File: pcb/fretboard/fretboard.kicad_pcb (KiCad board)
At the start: 2 copper layers, 46 x 186 mm, 101 parts, among them J1 Conn_01x05_Pin, J10 Conn_01x01_Pin, J11 Conn_01x01_Pin, J12 Conn_01x01_Pin, J13 Conn_01x01_Pin, J14 Conn_01x01_Pin, J15 Conn_01x01_Pin, J16 Conn_01x01_Pin, J17 Conn_01x01_Pin, J18 Conn_01x01_Pin, J19 Conn_01x01_Pin, J2 Conn_01x01_Pin, J20 Conn_01x01_Pin, J21 Conn_01x01_Pin, J22 Conn_01x01_Pin, J23 Conn_01x01_Pin, J24 Conn_01x01_Pin, J25 Conn_01x01_Pin, J26 Conn_01x01_Pin, J27 Conn_01x01_Pin, J28 Conn_01x01_Pin, J29 Conn_01x01_Pin, J3 Conn_01x01_Pin, J30 Conn_01x01_Pin, J31 Conn_01x01_Pin, J32 Conn_01x01_Pin, J33 Conn_01x01_Pin, J34 Conn_01x01_Pin, J35 Conn_01x01_Pin, J36 Conn_01x01_Pin, J37 Conn_01x01_Pin, J38 Conn_01x01_Pin, J39 Conn_01x01_Pin, J4 Conn_01x01_Pin, J40 Conn_01x01_Pin, J41 Conn_01x01_Pin, J42 Conn_01x01_Pin, J43 Conn_01x01_Pin, J44 Conn_01x01_Pin, J45 Conn_01x01_Pin, J46 Conn_01x01_Pin, J47 Conn_01x01_Pin, J48 Conn_01x01_Pin, J49 Conn_01x01_Pin, J5 Conn_01x01_Pin, J50 Conn_01x01_Pin, J51 Conn_01x01_Pin, J52 Conn_01x01_Pin, J53 Conn_01x01_Pin, J54 Conn_01x01_Pin, J55 Conn_01x01_Pin, J56 Conn_01x01_Pin, J57 Conn_01x01_Pin, J58 Conn_01x01_Pin, J59 Conn_01x01_Pin, J6 Conn_01x01_Pin, J60 Conn_01x01_Pin, J61 Conn_01x01_Pin, J7 Conn_01x01_Pin, J8 Conn_01x01_Pin, J9 Conn_01x01_Pin, U1 74HC165, U2 74HC165, U3 74HC165, U4 74HC165

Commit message: getting there
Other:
- board text added: "3.3V GND CLOCK LOAD DATA"
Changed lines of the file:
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@@
     )
     (stroke (width 0.15) (type solid)) (fill none) (layer "Edge.Cuts"))
+  (gr_text "3.3V\nGND\nCLOCK\nLOAD\nDATA" (at 42.164 181.9656) (layer "F.SilkS")
+    (effects (font (size 1.5 1.5) (thickness 0.3) bold) (justify right bottom))
+  )
 )

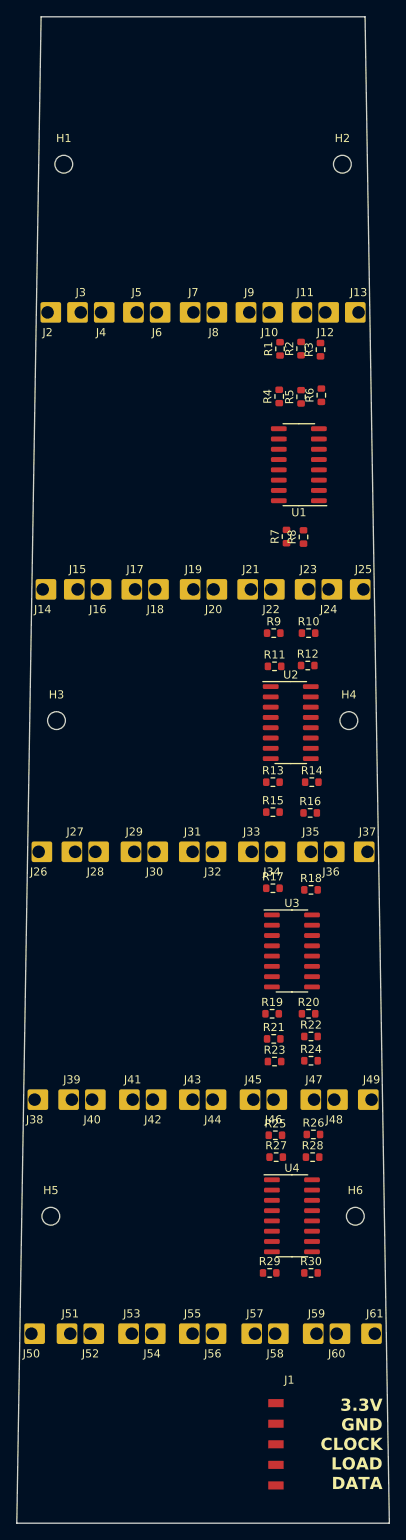
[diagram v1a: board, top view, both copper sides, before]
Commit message: fretboard routing
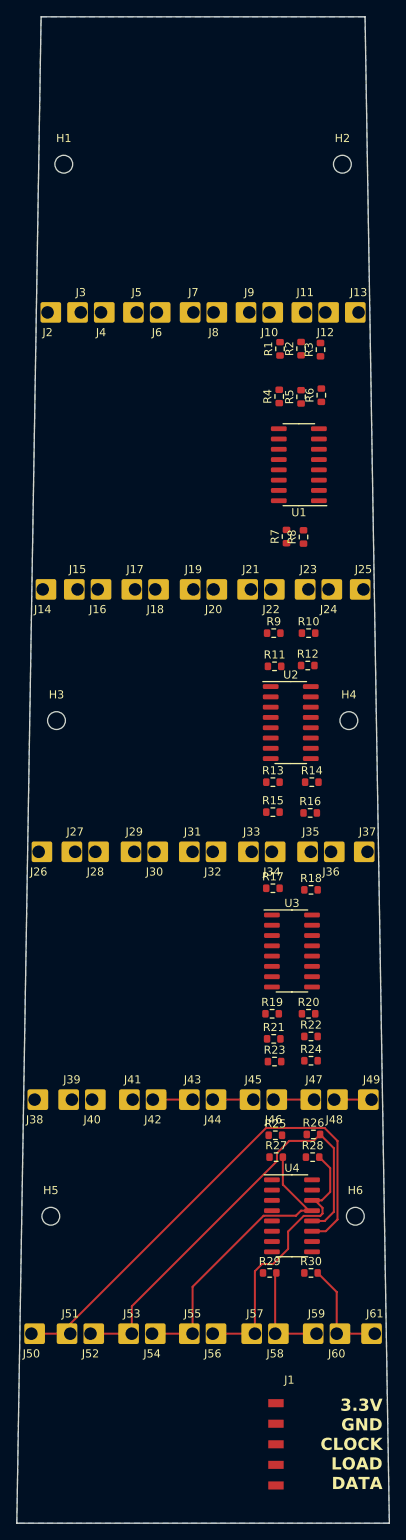
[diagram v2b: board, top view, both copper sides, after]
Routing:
- net Net-(J50-Pin_1): track 0.00 -> 63.1 mm
- net Net-(J52-Pin_1): track 0.00 -> 54.5 mm
- net Net-(J54-Pin_1): track 0.00 -> 37.8 mm
- net Net-(J56-Pin_1): track 0.00 -> 35.4 mm
- net Net-(J60-Pin_1): track 0.00 -> 13.2 mm
- net Net-(J58-Pin_1): track 0.00 -> 12.7 mm
- net Net-(J46-Pin_1): track 0.00 -> 5.00 mm
- net Net-(J44-Pin_1): track 0.00 -> 5.00 mm
- net Net-(J42-Pin_1): track 0.00 -> 4.90 mm
- net Net-(J48-Pin_1): track 0.00 -> 4.60 mm
- added copper zone on B.Cu, net GND
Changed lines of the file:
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@@
   )
   (setup
+    (stackup
+      (layer "F.SilkS" (type "Top Silk Screen"))
+      (layer "F.Paste" (type "Top Solder Paste"))
+      (layer "F.Mask" (type "Top Solder Mask") (thickness 0.01))
+      (layer "F.Cu" (type "copper") (thickness 0.035))
+      (layer "dielectric 1" (type "core") (thickness 1.51) (material "FR4") (epsilon_r 4.5) (loss_tangent 0.02))
+      (layer "B.Cu" (type "copper") (thickness 0.035))
+      (layer "B.Mask" (type "Bottom Solder Mask") (thickness 0.01))
+      (layer "B.Paste" (type "Bottom Solder Paste"))
+      (layer "B.SilkS" (type "Bottom Silk Screen"))
+      (copper_finish "None")
+      (dielectric_constraints no)
+    )
     (pad_to_mask_clearance 0)
     (pcbplotparams
@@
     (effects (font (size 1.5 1.5) (thickness 0.3) bold) (justify right bottom))
   )
+  (segment (start 26.2 133.7) (end 21.2 133.7) (width 0.25) (layer "F.Cu") (net 24))
+  (segment (start 33.7 133.7) (end 28.7 133.7) (width 0.25) (layer "F.Cu") (net 25))
+  (segment (start 40.8 133.7) (end 36.2 133.7) (width 0.25) (layer "F.Cu") (net 26))
+  (segment (start 27.782538 137.2) (end 35 137.2) (width 0.25) (layer "F.Cu") (net 27))
+  (segment (start 35.15 149.95) (end 33.45 149.95) (width 0.25) (layer "F.Cu") (net 27))
+  (segment (start 3.6 161.382538) (end 27.782538 137.2) (width 0.25) (layer "F.Cu") (net 27))
+  (segment (start 36.6 148.5) (end 35.15 149.95) (width 0.25) (layer "F.Cu") (net 27))
+  (segment (start 3.6 162.6) (end -1.2 162.6) (width 0.25) (layer "F.Cu") (net 27))
+  (segment (start 3.6 162.6) (end 3.6 161.382538) (width 0.25) (layer "F.Cu") (net 27))
+  (segment (start 36.6 138.8) (end 36.6 148.5) (width 0.25) (layer "F.Cu") (net 27))
+  (segment (start 35 137.2) (end 36.6 138.8) (width 0.25) (layer "F.Cu") (net 27))
+  (segment (start 33.65 138.8) (end 34.45 138) (width 0.25) (layer "F.Cu") (net 28))
+  (segment (start 36.15 139.7) (end 36.15 147.55) (width 0.25) (layer "F.Cu") (net 28))
+  (segment (start 29.125 141.292462) (end 29.125 140.307538) (width 0.25) (layer "F.Cu") (net 28))
+  (segment (start 11.2 162.6) (end 6.1 162.6) (width 0.25) (layer "F.Cu") (net 28))
+  (segment (start 30.632538 138.8) (end 33.65 138.8) (width 0.25) (layer "F.Cu") (net 28))
+  (segment (start 11.2 159.217462) (end 29.125 141.292462) (width 0.25) (layer "F.Cu") (net 28))
+  (segment (start 35.02 148.68) (end 33.45 148.68) (width 0.25) (layer "F.Cu") (net 28))
+  (segment (start 11.2 162.6) (end 11.2 159.217462) (width 0.25) (layer "F.Cu") (net 28))
+  (segment (start 29.125 140.307538) (end 30.632538 138.8) (width 0.25) (layer "F.Cu") (net 28))
+  (segment (start 34.45 138) (end 36.15 139.7) (width 0.25) (layer "F.Cu") (net 28))
+  (segment (start 36.15 147.55) (end 35.02 148.68) (width 0.25) (layer "F.Cu") (net 28))
+  (segment (start 32.09 147.41) (end 33.45 147.41) (width 0.25) (layer "F.Cu") (net 29))
+  (segment (start 29.85 140.8) (end 29.85 144.186751) (width 0.25) (layer "F.Cu") (net 29))
+  (segment (start 29.85 144.186751) (end 33.073249 147.41) (width 0.25) (layer "F.Cu") (net 29))
+  (segment (start 18.7 162.6) (end 13.7 162.6) (width 0.25) (layer "F.Cu") (net 29))
+  (segment (start 31.465 148.035) (end 32.09 147.41) (width 0.25) (layer "F.Cu") (net 29))
+  (segment (start 18.7 156.813249) (end 27.478249 148.035) (width 0.25) (layer "F.Cu") (net 29))
+  (segment (start 33.073249 147.41) (end 33.45 147.41) (width 0.25) (layer "F.Cu") (net 29))
+  (segment (start 27.478249 148.035) (end 31.465 148.035) (width 0.25) (layer "F.Cu") (net 29))
+  (segment (start 18.7 162.6) (end 18.7 156.813249) (width 0.25) (layer "F.Cu") (net 29))
+  (segment (start 33.826751 146.14) (end 34.75 147.063249) (width 0.25) (layer "F.Cu") (net 30))
+  (segment (start 34.471751 148.055) (end 32.428249 148.055) (width 0.25) (layer "F.Cu") (net 30))
+  (segment (start 27.282538 154) (end 26.4 154.882538) (width 0.25) (layer "F.Cu") (net 30))
+  (segment (start 26.4 154.882538) (end 26.4 162.6) (width 0.25) (layer "F.Cu") (net 30))
+  (segment (start 28.636751 154) (end 27.282538 154) (width 0.25) (layer "F.Cu") (net 30))
+  (segment (start 30.5 149.983249) (end 30.5 152.136751) (width 0.25) (layer "F.Cu") (net 30))
+  (segment (start 34.75 147.063249) (end 34.75 147.776751) (width 0.25) (layer "F.Cu") (net 30))
+  (segment (start 35.7 145.1) (end 35.7 142.15) (width 0.25) (layer "F.Cu") (net 30))
+  (segment (start 35.7 142.15) (end 34.35 140.8) (width 0.25) (layer "F.Cu") (net 30))
+  (segment (start 33.45 146.14) (end 33.826751 146.14) (width 0.25) (layer "F.Cu") (net 30))
+  (segment (start 34.66 146.14) (end 35.7 145.1) (width 0.25) (layer "F.Cu") (net 30))
+  (segment (start 30.5 152.136751) (end 28.636751 154) (width 0.25) (layer "F.Cu") (net 30))
+  (segment (start 26.4 162.6) (end 21.2 162.6) (width 0.25) (layer "F.Cu") (net 30))
+  (segment (start 33.45 146.14) (end 34.66 146.14) (width 0.25) (layer "F.Cu") (net 30))
+  (segment (start 34.75 147.776751) (end 34.471751 148.055) (width 0.25) (layer "F.Cu") (net 30))
+  (segment (start 32.428249 148.055) (end 30.5 149.983249) (width 0.25) (layer "F.Cu") (net 30))
+  (segment (start 36.5 157.45) (end 34.15 155.1) (width 0.25) (layer "F.Cu") (net 31))
+  (segment (start 41.2 162.6) (end 36.5 162.6) (width 0.25) (layer "F.Cu") (net 31))
+  (segment (start 36.5 162.6) (end 36.5 157.45) (width 0.25) (layer "F.Cu") (net 31))
+  (segment (start 18.7 133.7) (end 13.8 133.7) (width 0.25) (layer "F.Cu") (net 33))
+  (segment (start 28.9 155.25) (end 29.05 155.1) (width 0.25) (layer "F.Cu") (net 34))
+  (segment (start 34 162.6) (end 28.9 162.6) (width 0.25) (layer "F.Cu") (net 34))
+  (segment (start 28.9 162.6) (end 28.9 155.25) (width 0.25) (layer "F.Cu") (net 34))
+  (zone (net 2) (net_name "GND") (layer "B.Cu") (hatch edge 0.5)
+    (connect_pads (clearance 0.5))
+    (min_thickness 0.25) (filled_areas_thickness no)
+    (fill yes (thermal_gap 0.5) (thermal_bridge_width 0.5))
+    (polygon
+      (pts
+        (xy 0 0)
+        (xy 40 0)
+        (xy 43 186)
+        (xy -3 186)
+      )
+    )
+  )
 )

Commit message: faffing with fretboard
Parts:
- removed the J11 at (32.6, 36.5)
- removed the J13 at (39.2, 36.5)
- removed the J15 at (4.50, 70.7)
- removed the J17 at (11.6, 70.7)
- removed the J19 at (18.8, 70.7)
- removed the J21 at (25.9, 70.7)
- removed the J23 at (33.0, 70.7)
- removed the J25 at (39.8, 70.7)
- removed the J3 at (4.90, 36.5)
- removed J33, J35, J37, J39, J41, J43, J45, J47, J49, J50, J51, J52, J53, J54, J55, J56, J57, J58, J59, J60, J61: Conn_01x01_Pin, Bjarkar:Bjarkar_fret_connection
- removed the J5 at (11.8, 36.5)
- removed the J7 at (18.8, 36.5)
- removed the J9 at (25.7, 36.5)
- added J26: Conn_01x01_Pin, Bjarkar:Bjarkar_fret_connection, F.Cu at (1.00, 162.5)
- added J28: Conn_01x01_Pin, Bjarkar:Bjarkar_fret_connection, F.Cu at (16.2, 162.5)
- added J30: Conn_01x01_Pin, Bjarkar:Bjarkar_fret_connection, F.Cu at (31.4, 162.5)
- moved J31 62.8 mm to (39.0, 162.5)
- moved J29 60.7 mm to (23.8, 162.5)
- moved J27 59.6 mm to (8.60, 162.5)
- moved R26 14.0 mm to (33.0, 152.0)
- moved R25 13.9 mm to (29.0, 152.0)
- moved R28 13.2 mm to (33.0, 154.0)
- moved R27 13.2 mm to (29.0, 154.0)
- moved R3 7.37 mm to (29.0, 46.0), turned to 0 degrees
- moved U4 4.05 mm to (31.0, 144.0)
- moved R4 3.70 mm to (33.0, 46.0), turned to 0 degrees
- moved R5 3.28 mm to (29.0, 48.0), turned to 0 degrees
- moved R2 3.16 mm to (33.0, 44.0), turned to 0 degrees
- moved R1 3.04 mm to (29.0, 44.0), turned to 0 degrees
- moved J21 2.50 mm to (8.80, 133.7)
- moved J23 2.50 mm to (23.7, 133.7)
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- renumbered J18 to J10, J20 to J11, J22 to J12, J24 to J13, J26 to J14, J28 to J15, J30 to J16, J32 to J17, J34 to J18, J36 to J19, J38 to J20, J40 to J21, J42 to J22, J44 to J23, J46 to J24, J48 to J25, J4 to J3, J6 to J4, J8 to J5, J10 to J6, J12 to J7, J14 to J8, J16 to J9
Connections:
- J14 pad 1: Net-(J26-Pin_1) (its old number) -> Net-(J14-Pin_1)
- J15 pad 1: Net-(J28-Pin_1) (its old number) -> Net-(J15-Pin_1)
- J16 pad 1: Net-(J30-Pin_1) (its old number) -> Net-(J16-Pin_1)
- J27 pad 1: Net-(J26-Pin_1) (its old number) -> Net-(J27-Pin_1)
- J29 pad 1: Net-(J28-Pin_1) (its old number) -> Net-(J29-Pin_1)
- J31 pad 1: Net-(J30-Pin_1) (its old number) -> Net-(J31-Pin_1)
- R13 pad 2: Net-(J26-Pin_1) (its old number) -> Net-(J14-Pin_1)
- R14 pad 2: Net-(J28-Pin_1) (its old number) -> Net-(J15-Pin_1)
- R15 pad 2: Net-(J30-Pin_1) (its old number) -> Net-(J16-Pin_1)
- R26 pad 2: Net-(J52-Pin_1) -> Net-(J27-Pin_1)
- R28 pad 2: Net-(J56-Pin_1) -> Net-(J29-Pin_1)
- R30 pad 2: Net-(J60-Pin_1) -> Net-(J31-Pin_1)
- U2 pad 3: Net-(J26-Pin_1) (its old number) -> Net-(J14-Pin_1)
- U2 pad 4: Net-(J28-Pin_1) (its old number) -> Net-(J15-Pin_1)
- U2 pad 5: Net-(J30-Pin_1) (its old number) -> Net-(J16-Pin_1)
- U4 pad 12: Net-(J52-Pin_1) -> Net-(J27-Pin_1)
- U4 pad 14: Net-(J56-Pin_1) -> Net-(J29-Pin_1)
- U4 pad 4: Net-(J60-Pin_1) -> Net-(J31-Pin_1)
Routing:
- net Net-(J26-Pin_1): track 63.1 -> 0.00 mm
- net Net-(J52-Pin_1): track 54.5 -> 0.00 mm
- net Net-(J28-Pin_1): track 37.8 -> 0.00 mm
- net Net-(J56-Pin_1): track 35.4 -> 0.00 mm
- net Net-(J60-Pin_1): track 13.2 -> 0.00 mm
- net Net-(J30-Pin_1): track 12.7 -> 0.00 mm
- net Net-(J24-Pin_1): track 5.00 -> 0.00 mm
- net Net-(J23-Pin_1): track 5.00 -> 0.00 mm
- net Net-(J22-Pin_1): track 4.90 -> 0.00 mm
- net Net-(J25-Pin_1): track 4.60 -> 0.00 mm

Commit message: fretboard routing done
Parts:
- moved J2 0.10 mm to (2.90, 36.4)
- moved J3 0.10 mm to (9.75, 36.4)
- moved J4 0.10 mm to (16.6, 36.4)
- moved J5 0.10 mm to (23.4, 36.4)
- moved J6 0.10 mm to (30.2, 36.4)
- moved J7 0.10 mm to (37.1, 36.4)
- moved J20 0.10 mm to (1.35, 133.6)
- moved J21 0.10 mm to (8.80, 133.6)
- moved J22 0.10 mm to (16.2, 133.6)
- moved J23 0.10 mm to (23.7, 133.6)
- moved J24 0.10 mm to (31.2, 133.6)
- moved J25 0.10 mm to (38.6, 133.6)
- moved J19 0.05 mm to (38.1, 103.1)
- turned U1 to 0 degrees
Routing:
- net +3.3V: track 0.00 -> 277.7 mm
- net 165_LOAD: track 0.00 -> 195.3 mm, vias 0 -> 6
- net 165_CLOCK: track 0.00 -> 176.8 mm
- net Net-(J2-Pin_1): track 0.00 -> 50.5 mm, vias 0 -> 2
- net Net-(J20-Pin_1): track 0.00 -> 45.9 mm, vias 0 -> 3
- net Net-(J21-Pin_1): track 0.00 -> 45.6 mm, vias 0 -> 1
- net Net-(J26-Pin_1): track 0.00 -> 45.4 mm, vias 0 -> 3
- net Net-(J27-Pin_1): track 0.00 -> 44.3 mm, vias 0 -> 3
- net Net-(J3-Pin_1): track 0.00 -> 44.2 mm, vias 0 -> 2
- net Net-(J14-Pin_1): track 0.00 -> 43.6 mm, vias 0 -> 1
- net Net-(J5-Pin_1): track 0.00 -> 41.9 mm, vias 0 -> 2
- net Net-(J22-Pin_1): track 0.00 -> 41.8 mm, vias 0 -> 1
- net /ShiftReg4/DATA_OUT: track 0.00 -> 41.5 mm
- net Net-(J15-Pin_1): track 0.00 -> 41.3 mm, vias 0 -> 1
- net Net-(J8-Pin_1): track 0.00 -> 41.1 mm, vias 0 -> 1
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
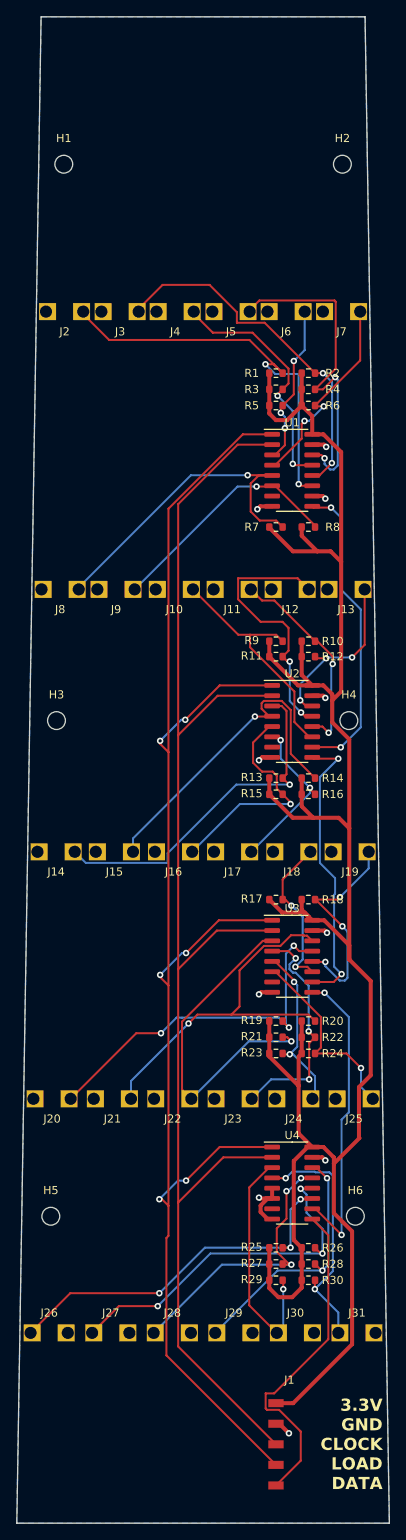
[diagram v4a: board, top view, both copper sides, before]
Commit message: fretboard finished
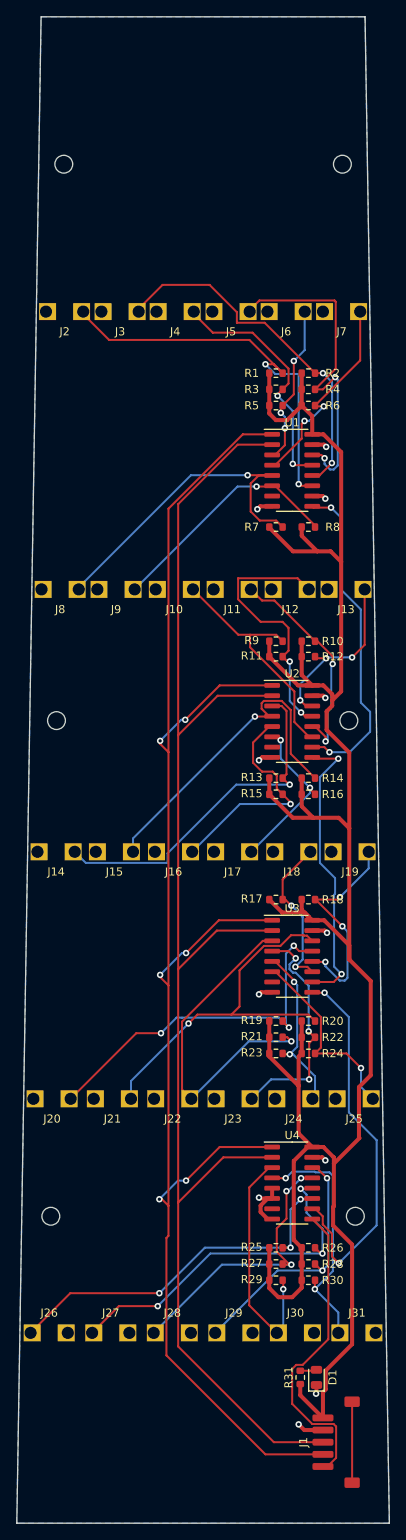
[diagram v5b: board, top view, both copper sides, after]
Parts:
- added D1: LED, LED_SMD:LED_0805_2012Metric, F.Cu at (34.0, 168.0)
- added R31: 220R, Resistor_SMD:R_0603_1608Metric, F.Cu at (32.0, 168.0)
- H1, H2, H3, H4, H5, H6: footprint MountingHole:MountingHole_2.2mm_M2 -> Bjarkar:MountingHole_2.2mm_M2_countersunk; moved to B.Cu
- J1: value Conn_01x05_Pin -> Conn_01x06_Pin; footprint Bjarkar:bjarkar_fretboard_header -> Bjarkar:jst zh fretboard connector
- moved J1 6.36 mm to (37.0, 176.0), turned to 90 degrees
- turned H1 to 180 degrees
- turned H2 to 180 degrees
- turned H3 to 180 degrees
- turned H4 to 180 degrees
- turned H5 to 180 degrees
- turned H6 to 180 degrees
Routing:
- net unconnected-(J1-Pin_6-Pad6): track 0.00 -> 10.0 mm
- net /ShiftReg3/DATA_OUT: track 38.0 -> 47.8 mm
- net 165_CLOCK: track 176.8 -> 182.5 mm
- net 165_LOAD: track 195.3 -> 200.5 mm
- net +3.3V: track 277.7 -> 281.9 mm
- net /ShiftReg4/DATA_OUT: track 41.5 -> 38.5 mm
- net /ShiftReg1/DATA_OUT: track 38.1 -> 40.5 mm
- net GND: track 23.9 -> 26.2 mm, vias 10 -> 11
- net Net-(D1-A): track 0.00 -> 2.05 mm
- net Net-(J11-Pin_1): track 25.5 -> 27.1 mm
